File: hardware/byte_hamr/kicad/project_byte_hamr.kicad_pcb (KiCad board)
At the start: 4 copper layers, 103.8 x 67.3 mm, 93 parts, among them J1 Conn_02x20_Odd_Even, J3 Bus_Apple_II_Card_Side, J4 CONN_02X03, J6 Conn_02x03_Odd_Even, U1 LFE5U-85F-8BG381I, U10 IS25LP128F-JBLE, U11 SN74LVC8T245, U12 SN74LVC8T245, U13 SN74LVC8T245, U14 SN74LVC8T245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

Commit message: Updates WIP to Rev.2
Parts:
- moved US1 99.3 mm to (135.1, 73.0), turned to -90 degrees
- moved D1 88.1 mm to (144.1, 73.2)
- moved G*** 4.13 mm to (150.9, 63.0)
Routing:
- net /usb/FTD+: track 45.2 -> 69.7 mm
- net /usb/FTD-: track 46.4 -> 68.3 mm
- net GND: track 343.2 -> 349.4 mm
- net USB5V: track 7.72 -> 6.50 mm
- net +5V: track 78.8 -> 77.9 mm
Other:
- board text added: "-12v"
- board text added: "-5v"
- board text added: "12v"
- board text added: "3v3"
- board text added: "5v"

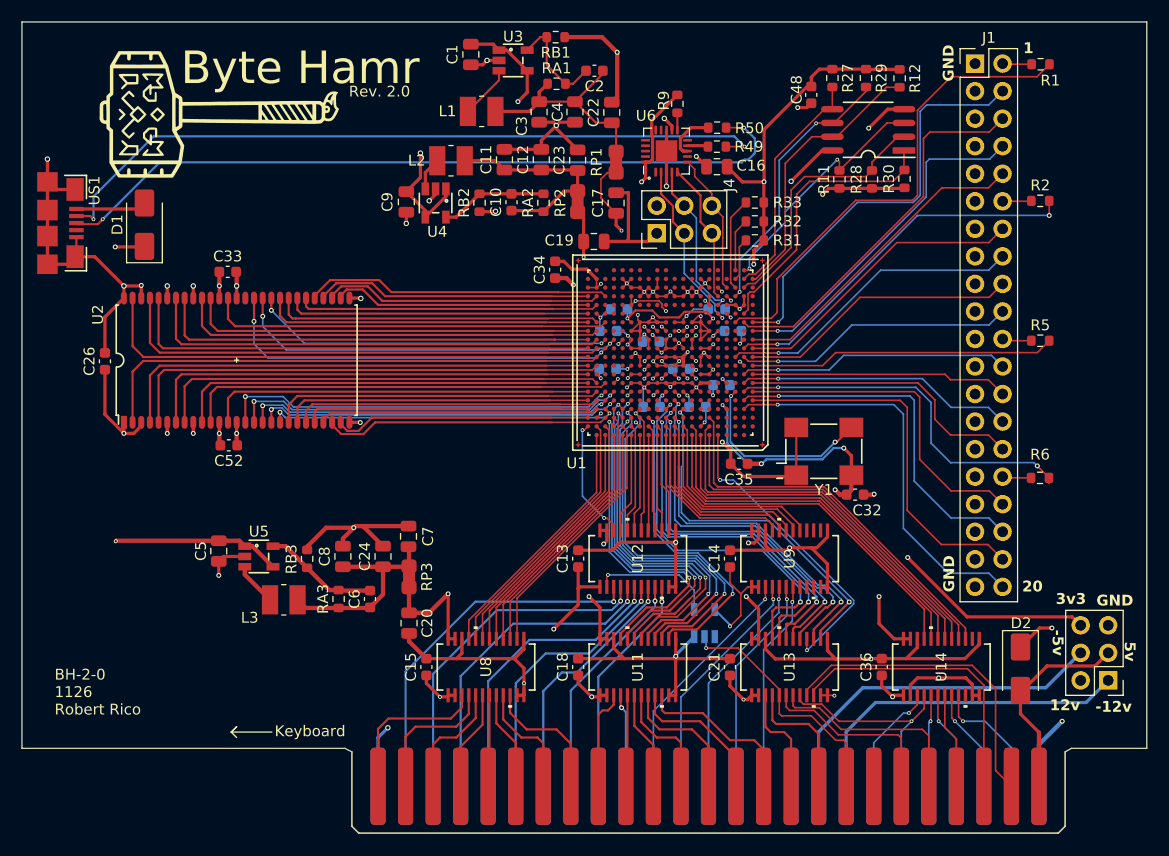
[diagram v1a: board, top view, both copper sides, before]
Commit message: Refine hardware design and documentation for Revision 2.0
Updates footprint library references to use local Apple II connector footprints and adjusts component placements and trace routing across the PCB. Silkscreen date codes and text sizes have been updated, and a correction was made to the flash memory capacity notation in the README.
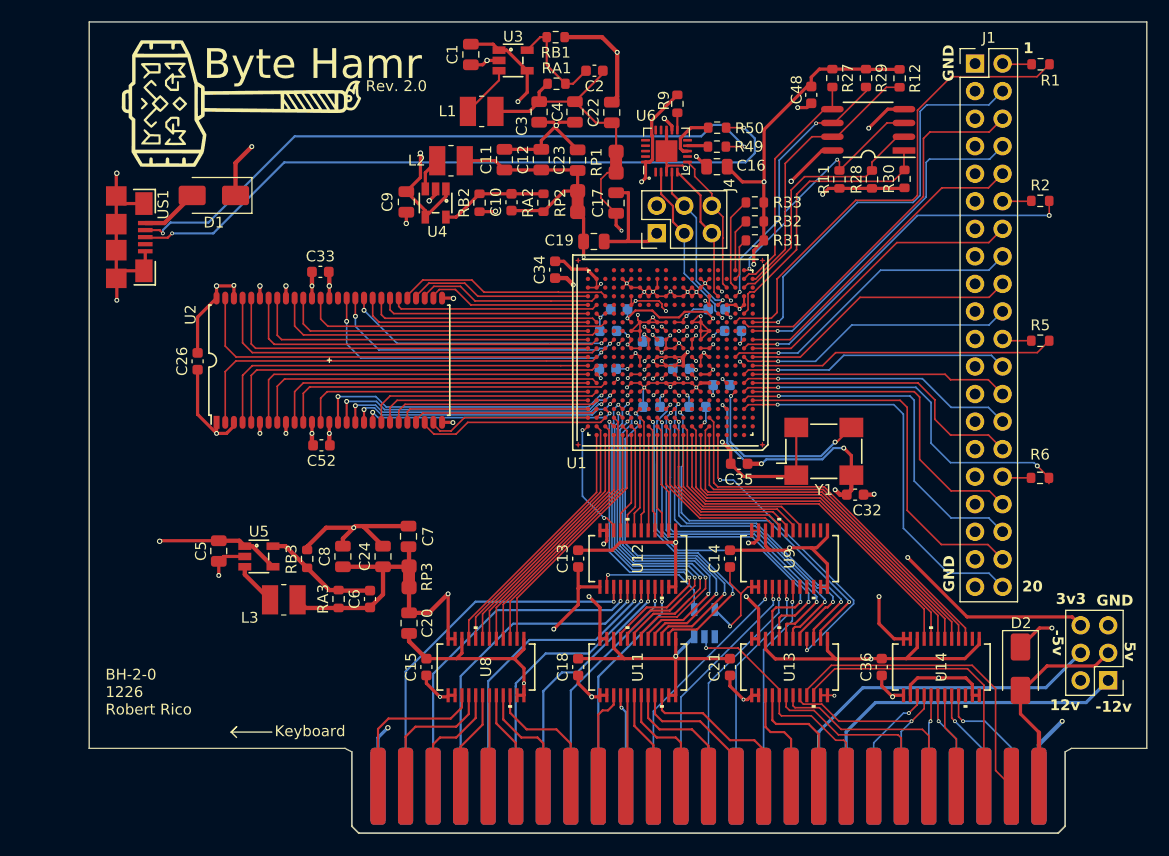
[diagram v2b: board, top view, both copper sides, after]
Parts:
- J3: footprint PCM_MA_Connector_AppleII:Peripheral_Bus_Edge -> com_github_markadev_KiCad-AppleII:Peripheral_Bus_Edge
- moved C26 8.55 mm to (149.0, 85.8)
- moved C33 8.55 mm to (160.3, 77.5)
- moved C52 8.55 mm to (160.4, 93.5)
- moved U2 8.55 mm to (161.1, 85.7)
- moved D1 6.95 mm to (150.5, 70.5), turned to 180 degrees
- moved US1 6.48 mm to (141.5, 74.3)
- moved G*** 2.28 mm to (153.0, 62.0)
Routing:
- net SDRAM_D2: track 45.1 -> 36.6 mm
- net SDRAM_D11: track 40.8 -> 32.3 mm
- net SDRAM_DQM0: track 36.6 -> 28.1 mm
- net SDRAM_D10: track 39.5 -> 30.9 mm
- net SDRAM_nCAS: track 33.9 -> 25.3 mm
- net SDRAM_nWE: track 36.2 -> 27.6 mm
- net SDRAM_nCS: track 32.3 -> 23.7 mm
- net SDRAM_D9: track 37.5 -> 28.9 mm
- net SDRAM_D6: track 39.5 -> 30.9 mm
- net SDRAM_D3: track 42.1 -> 33.6 mm
- net SDRAM_D15: track 46.8 -> 38.3 mm
- net SDRAM_D14: track 45.9 -> 37.3 mm
- net SDRAM_D12: track 42.9 -> 34.4 mm
- net SDRAM_D0: track 48.0 -> 39.5 mm
- net SDRAM_BA1: track 28.4 -> 19.9 mm
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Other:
- board size 103.8 x 67.3 mm -> 97.6 x 67.3 mm
- board text added: "BH-2-0 1226 Robert Rico"
- board text removed: "BH-2-0 1126 Robert Rico"
